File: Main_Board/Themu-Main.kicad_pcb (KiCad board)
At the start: 2 copper layers, 49.5 x 23.5 mm, 50 parts, among them J1 USB_B_Micro, J2 Conn_01x02, J3 Conn_01x08, Q1 mmbt2222, Q2 mmbt2222, Q3 DMG2305U, U1 CP2104, U2 AP2112K-3.3, U3 ESP32-WROOM-32, U4 MCP73831-2-OT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

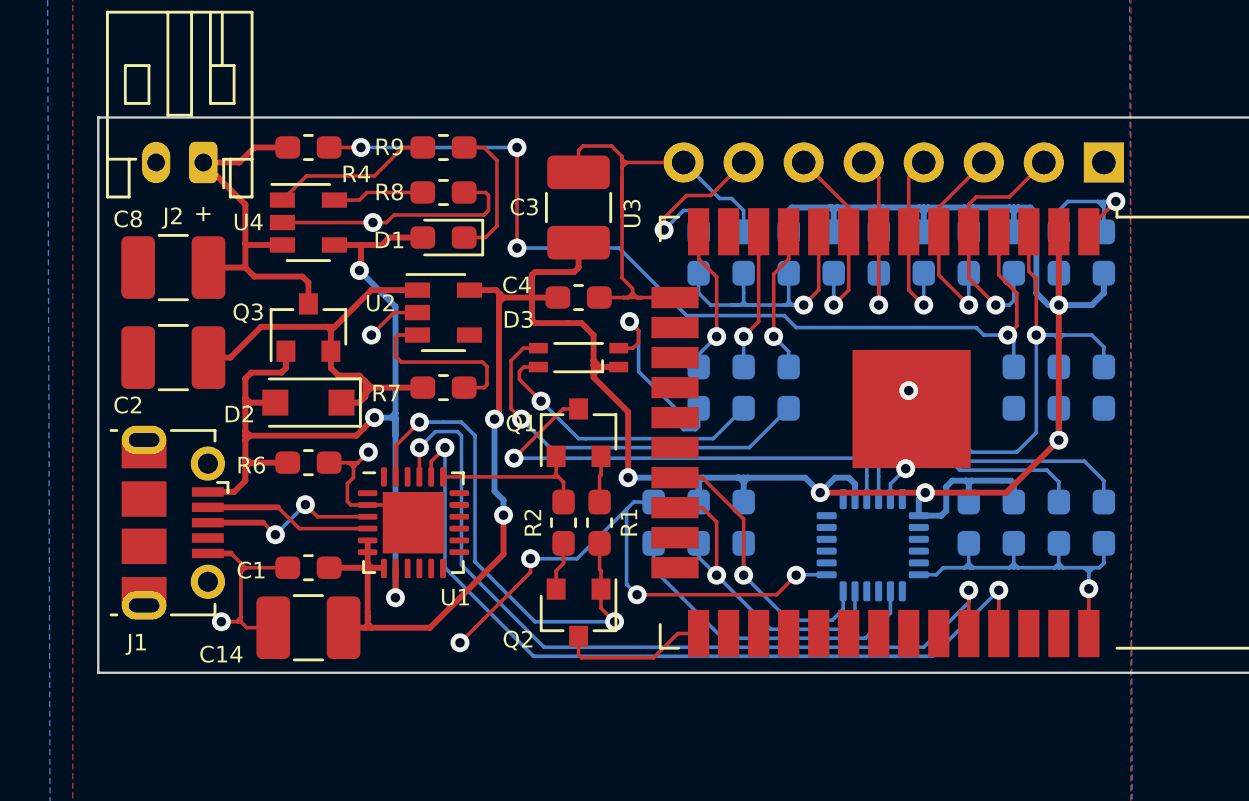
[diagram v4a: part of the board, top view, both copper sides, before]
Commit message: Changing I2C pins
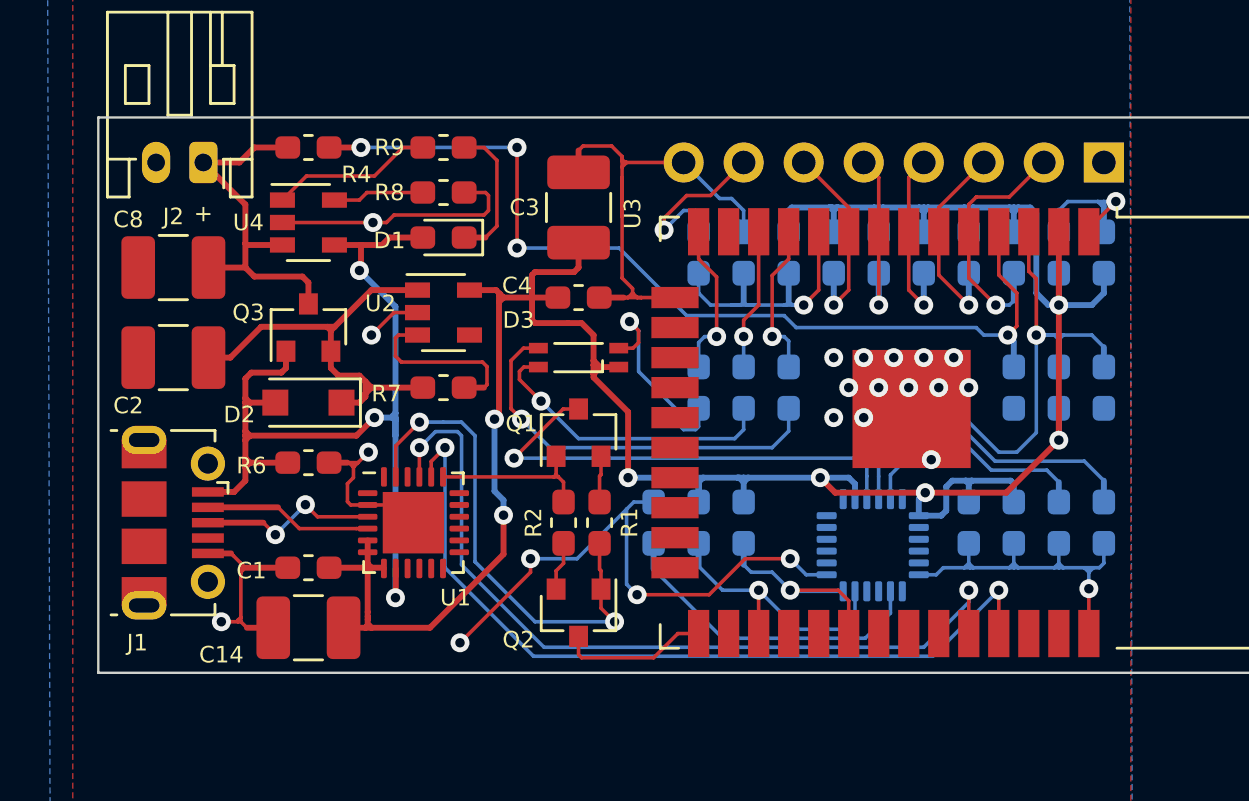
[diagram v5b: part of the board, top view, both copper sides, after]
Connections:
- J1 pad 4: (no net) -> Net-(J1-Pad4)
- J3 pad 1: (no net) -> Net-(J3-Pad1)
- U1 pad 1: (no net) -> Net-(U1-Pad1)
- U1 pad 10: (no net) -> Net-(U1-Pad10)
- U1 pad 11: (no net) -> Net-(U1-Pad11)
- U1 pad 12: (no net) -> Net-(U1-Pad12)
- U1 pad 13: (no net) -> Net-(U1-Pad13)
- U1 pad 14: (no net) -> Net-(U1-Pad14)
- U1 pad 15: (no net) -> Net-(U1-Pad15)
- U1 pad 16: (no net) -> Net-(U1-Pad16)
- U1 pad 17: (no net) -> Net-(U1-Pad17)
- U1 pad 18: (no net) -> Net-(U1-Pad18)
- U1 pad 22: (no net) -> Net-(U1-Pad22)
- U1 pad 24: (no net) -> Net-(U1-Pad24)
- U1 pad 9: (no net) -> Net-(U1-Pad9)
- U2 pad 4: (no net) -> Net-(U2-Pad4)
- U3 pad 13: (no net) -> Net-(U3-Pad13)
- U3 pad 16: (no net) -> Net-(U3-Pad16)
- U3 pad 17: (no net) -> Net-(U3-Pad17)
- U3 pad 18: (no net) -> Net-(U3-Pad18)
- U3 pad 19: (no net) -> Net-(U3-Pad19)
- U3 pad 20: (no net) -> Net-(U3-Pad20)
- U3 pad 21: /ESP32-WROOM-32/SDA -> Net-(U3-Pad21)
- U3 pad 22: /ESP32-WROOM-32/SCL -> Net-(U3-Pad22)
- U3 pad 23: (no net) -> Net-(U3-Pad23)
- U3 pad 24: (no net) -> Net-(U3-Pad24)
- U3 pad 26: (no net) -> Net-(U3-Pad26)
- U3 pad 27: (no net) -> /ESP32-WROOM-32/SCL
- U3 pad 28: (no net) -> Net-(U3-Pad28)
- U3 pad 29: (no net) -> Net-(U3-Pad29)
- U3 pad 30: (no net) -> /ESP32-WROOM-32/SDA
- U3 pad 31: (no net) -> Net-(U3-Pad31)
- U3 pad 32: (no net) -> Net-(U3-Pad32)
- U3 pad 33: (no net) -> Net-(U3-Pad33)
- U3 pad 36: (no net) -> Net-(U3-Pad36)
- U3 pad 37: (no net) -> Net-(U3-Pad37)
- U5 pad 12: (no net) -> /Peripherials/INT
- U5 pad 6: (no net) -> /Peripherials/XDA
- U5 pad 7: (no net) -> /Peripherials/XCL
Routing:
- net /ESP32-WROOM-32/SDA: track 13.3 -> 9.64 mm
- net /ESP32-WROOM-32/SCL: track 14.0 -> 11.7 mm
- net /ESP32-WROOM-32/EN: track 41.8 -> 42.3 mm
- net /Peripherials/AD0: track 13.4 -> 14.0 mm
- net /Peripherials/REGOUT: track 10.7 -> 11.3 mm
- net Net-(D3-Pad4): track 16.5 -> 17.1 mm
- net Net-(D3-Pad1): track 12.3 -> 12.8 mm
- net GND: track 103.1 -> 102.9 mm, vias 12 -> 23
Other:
- board text added: "*Placement grid: 25 mils (0.635 mm) (60 mils between R1 and R2) *Routing grid: 2.5 mils (0.0635 mm) *Tracks width: 6 mils (0.1524 mm) *Clearance: 8 mils (0.2032 mm) *Vias drill/size: 15.748/31.496 mils (0.4/0.8 mm) *Surface Finish: HASL Lead Free. *Copper-to-edge distance: 20 mils (0.51 mm) *Board size: 1950x925 mils (49.5x23.5 mm)"
- board text added: "Rev: 04 Diseño Argentino"
- board text removed: "*Placement grid: 25 mils (0.635 mm) (60 mils between R1 and R2) *Routing grid: 2.5 mils (0.0635 mm) *Tracks width: 6 mils (0.1524 mm) *Clearance: 8 mils (0.2032 mm) *Vias drill/size: 15.748/31.496 mils (0.4/0.8 mm) *Surface Finish: HASL Lead Free. *Copper-to-edge distance: 20 mils (0.51 mm) *Board size: 1950x925 mils (49.5/23.5 mm)"
- board text removed: "Rev: 03 Diseño Argentino"

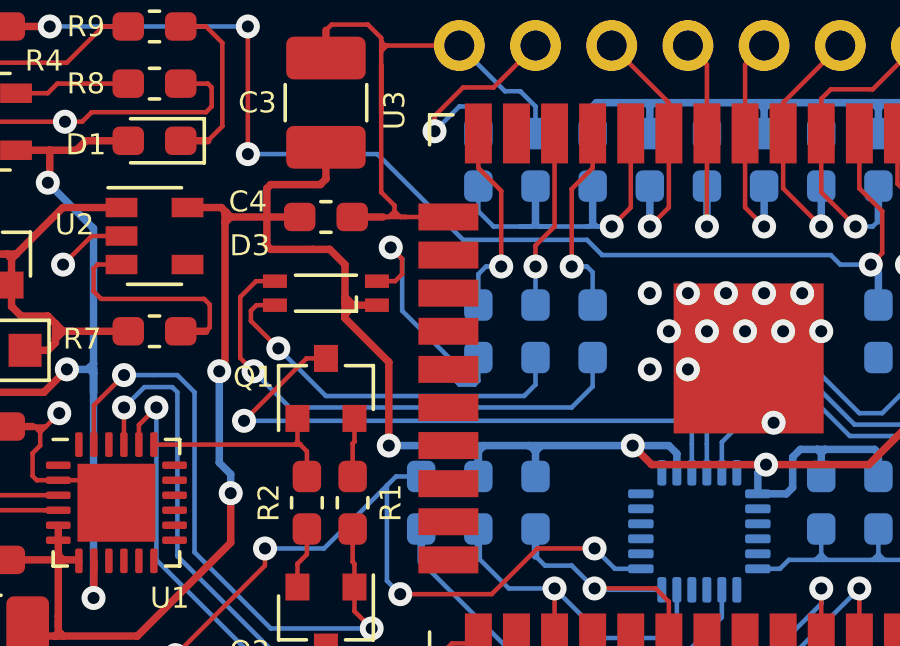
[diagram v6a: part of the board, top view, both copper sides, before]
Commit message: New D3 footprint and model
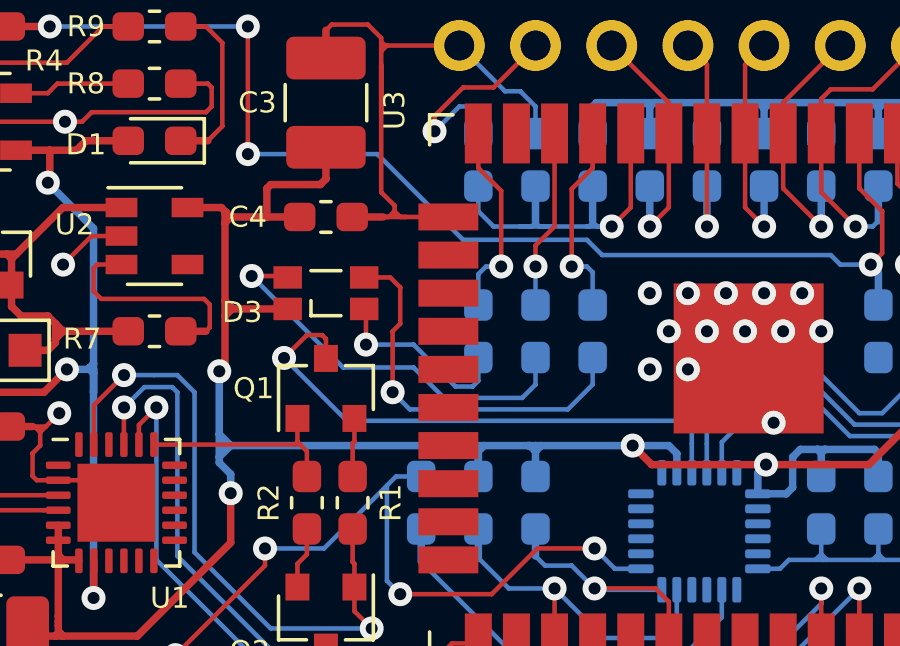
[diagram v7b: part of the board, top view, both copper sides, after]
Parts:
- D3: value LED_RABG -> LED_BARG; footprint Main_Board:LED_QBLP655R_RGB -> Main_Board:LED-160-80180
- turned D3 to 0 degrees
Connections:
- R21 pad 2: Net-(D3-Pad1) -> Net-(D3-Pad3)
- R3 pad 2: Net-(D3-Pad3) -> Net-(D3-Pad1)
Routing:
- net Net-(D3-Pad1): track 12.8 -> 6.39 mm
- net Net-(D3-Pad3): track 8.97 -> 13.5 mm
- net Net-(D3-Pad4): track 17.1 -> 13.1 mm
- net +3V3: track 119.2 -> 116.2 mm, vias 7 -> 6
- net /ESP32-WROOM-32/EN: track 42.3 -> 40.7 mm

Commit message: C2, C3, C8 and C14 footprints and packages changed from 1210 to 0603 (#11)
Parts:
- C14, C2, C3, C8: footprint Capacitor_SMD:C_1210_3225Metric_Pad1.42x2.65mm_HandSolder -> Capacitor_SMD:C_0603_1608Metric_Pad1.08x0.95mm_HandSolder
- moved C3 1.91 mm to (64.8, 84.5), turned to 0 degrees
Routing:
- net GND: track 102.9 -> 98.1 mm
- net /ESP32-WROOM-32/ADC1_CH0: track 40.8 -> 39.8 mm
- net /Power/RegIn: track 18.5 -> 19.1 mm
- net +BATT: track 16.0 -> 16.6 mm
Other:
- board text added: "Rev: 4.1 Diseño Argentino"
- board text removed: "Rev: 04 Diseño Argentino"
